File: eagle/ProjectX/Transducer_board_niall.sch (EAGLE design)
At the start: 105 parts, among them T1 MA40S4S, T10 MA40S4S, T100 MA40S4S, T11 MA40S4S, T12 MA40S4S, T13 MA40S4S, T14 MA40S4S, T15 MA40S4S, T16 MA40S4S, T17 MA40S4S, T18 MA40S4S, T19 MA40S4S, T2 MA40S4S, T20 MA40S4S, T21 MA40S4S, T22 MA40S4S, T23 MA40S4S, T24 MA40S4S, T25 MA40S4S, T26 MA40S4S, T27 MA40S4S, T28 MA40S4S, T29 MA40S4S, T3 MA40S4S, T30 MA40S4S, T31 MA40S4S, T32 MA40S4S, T33 MA40S4S, T34 MA40S4S, T35 MA40S4S, T36 MA40S4S, T37 MA40S4S, T38 MA40S4S, T39 MA40S4S, T4 MA40S4S, T40 MA40S4S, T41 MA40S4S, T42 MA40S4S, T43 MA40S4S, T44 MA40S4S, T45 MA40S4S, T46 MA40S4S, T47 MA40S4S, T48 MA40S4S, T49 MA40S4S, T5 MA40S4S, T50 MA40S4S, T51 MA40S4S, T52 MA40S4S, T53 MA40S4S, T54 MA40S4S, T55 MA40S4S, T56 MA40S4S, T57 MA40S4S, T58 MA40S4S, T59 MA40S4S, T6 MA40S4S, T60 MA40S4S, T61 MA40S4S, T62 MA40S4S, T63 MA40S4S, T64 MA40S4S, T65 MA40S4S, T66 MA40S4S, T67 MA40S4S, T68 MA40S4S, T69 MA40S4S, T7 MA40S4S, T70 MA40S4S, T71 MA40S4S, T72 MA40S4S, T73 MA40S4S, T74 MA40S4S, T75 MA40S4S, T76 MA40S4S, T77 MA40S4S, T78 MA40S4S, T79 MA40S4S, T8 MA40S4S, T80 MA40S4S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

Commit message: Niall new board stuff
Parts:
- removed TRANSDUCERS_1, TRANSDUCERS_2, TRANSDUCERS_3, TRANSDUCERS_4, TRANSDUCERS_6: 40_PIN_SMD, Parts:40_PIN_SMD
- added X1, X2, X3, X4, X5: PHB_1MM27_2X20_SNS, _hhn_con_pinhead_box_1mm27:PHB_1MM27_2X20_SNS
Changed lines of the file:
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@@
 <parts>
 <part name="T1" library="Parts" deviceset="MA40S4S" device=""/>
-<part name="TRANSDUCERS_4" library="Parts" deviceset="40_PIN_SMD" device=""/>
-<part name="TRANSDUCERS_3" library="Parts" deviceset="40_PIN_SMD" device=""/>
-<part name="TRANSDUCERS_2" library="Parts" deviceset="40_PIN_SMD" device=""/>
-<part name="TRANSDUCERS_1" library="Parts" deviceset="40_PIN_SMD" device=""/>
 <part name="T2" library="Parts" deviceset="MA40S4S" device=""/>
 <part name="T3" library="Parts" deviceset="MA40S4S" device=""/>
@@
 <part name="T99" library="Parts" deviceset="MA40S4S" device=""/>
 <part name="T100" library="Parts" deviceset="MA40S4S" device=""/>
-<part name="TRANSDUCERS_6" library="Parts" deviceset="40_PIN_SMD" device=""/>
+<part name="X1" library="_hhn_con_pinhead_box_1mm27" deviceset="PHB_1MM27_2X20_*" device="SNS"/>
+<part name="X2" library="_hhn_con_pinhead_box_1mm27" deviceset="PHB_1MM27_2X20_*" device="SNS"/>
+<part name="X3" library="_hhn_con_pinhead_box_1mm27" deviceset="PHB_1MM27_2X20_*" device="SNS"/>
+<part name="X4" library="_hhn_con_pinhead_box_1mm27" deviceset="PHB_1MM27_2X20_*" device="SNS"/>
+<part name="X5" library="_hhn_con_pinhead_box_1mm27" deviceset="PHB_1MM27_2X20_*" device="SNS"/>
 </parts>
 <sheets>
@@
 <instances>
 <instance part="T1" gate="G$1" x="-12.7" y="299.72"/>
-<instance part="TRANSDUCERS_4" gate="G$1" x="175.26" y="27.94" rot="MR0">
-<attribute name="NAME" x="225.298" y="48.26" size="1.778" layer="94" rot="MR0"/>
-</instance>
-<instance part="TRANSDUCERS_3" gate="G$1" x="106.68" y="25.4" rot="MR0">
-<attribute name="NAME" x="156.718" y="45.72" size="1.778" layer="94" rot="MR0"/>
-</instance>
-<instance part="TRANSDUCERS_2" gate="G$1" x="40.64" y="25.4" rot="MR0">
-<attribute name="NAME" x="90.678" y="45.72" size="1.778" layer="94" rot="MR0"/>
-</instance>
-<instance part="TRANSDUCERS_1" gate="G$1" x="-25.4" y="25.4" rot="MR0">
-<attribute name="NAME" x="24.638" y="45.72" size="1.778" layer="94" rot="MR0"/>
-</instance>
 <instance part="T2" gate="G$1" x="10.16" y="299.72"/>
 <instance part="T3" gate="G$1" x="33.02" y="299.72"/>
@@
 <instance part="T99" gate="G$1" x="170.18" y="132.08"/>
 <instance part="T100" gate="G$1" x="195.58" y="132.08"/>
-<instance part="TRANSDUCERS_6" gate="G$1" x="370.84" y="15.24" rot="MR90">
-<attribute name="NAME" x="391.16" y="-34.798" size="1.778" layer="94" rot="MR90"/>
-</instance>
+<instance part="X1" gate="G$1" x="-50.8" y="55.88"/>
+<instance part="X2" gate="G$1" x="-15.24" y="55.88"/>
+<instance part="X3" gate="G$1" x="30.48" y="55.88"/>
+<instance part="X4" gate="G$1" x="78.74" y="55.88"/>
+<instance part="X5" gate="G$1" x="121.92" y="55.88"/>
 </instances>
 <busses>

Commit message: Niall Boards new layout that should slot together
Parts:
- removed X1, X2, X3, X4, X5: PHB_1MM27_2X20_SNS, _hhn_con_pinhead_box_1mm27:PHB_1MM27_2X20_SNS
- added 1, 2, 3, 4: PHB_1MM27_2X25_SNS, _hhn_con_pinhead_box_1mm27:PHB_1MM27_2X25_SNS
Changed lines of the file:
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@@
 <part name="T99" library="Parts" deviceset="MA40S4S" device=""/>
 <part name="T100" library="Parts" deviceset="MA40S4S" device=""/>
-<part name="X1" library="_hhn_con_pinhead_box_1mm27" deviceset="PHB_1MM27_2X20_*" device="SNS"/>
-<part name="X2" library="_hhn_con_pinhead_box_1mm27" deviceset="PHB_1MM27_2X20_*" device="SNS"/>
-<part name="X3" library="_hhn_con_pinhead_box_1mm27" deviceset="PHB_1MM27_2X20_*" device="SNS"/>
-<part name="X4" library="_hhn_con_pinhead_box_1mm27" deviceset="PHB_1MM27_2X20_*" device="SNS"/>
-<part name="X5" library="_hhn_con_pinhead_box_1mm27" deviceset="PHB_1MM27_2X20_*" device="SNS"/>
+<part name="1" library="_hhn_con_pinhead_box_1mm27" deviceset="PHB_1MM27_2X25_*" device="SNS"/>
+<part name="2" library="_hhn_con_pinhead_box_1mm27" deviceset="PHB_1MM27_2X25_*" device="SNS"/>
+<part name="3" library="_hhn_con_pinhead_box_1mm27" deviceset="PHB_1MM27_2X25_*" device="SNS"/>
+<part name="4" library="_hhn_con_pinhead_box_1mm27" deviceset="PHB_1MM27_2X25_*" device="SNS"/>
 </parts>
 <sheets>
@@
 <instance part="T99" gate="G$1" x="170.18" y="132.08"/>
 <instance part="T100" gate="G$1" x="195.58" y="132.08"/>
-<instance part="X1" gate="G$1" x="-50.8" y="55.88"/>
-<instance part="X2" gate="G$1" x="-15.24" y="55.88"/>
-<instance part="X3" gate="G$1" x="30.48" y="55.88"/>
-<instance part="X4" gate="G$1" x="78.74" y="55.88"/>
-<instance part="X5" gate="G$1" x="121.92" y="55.88"/>
+<instance part="1" gate="G$1" x="-106.68" y="248.92" rot="R90"/>
+<instance part="2" gate="G$1" x="-205.74" y="162.56"/>
+<instance part="3" gate="G$1" x="-142.24" y="162.56"/>
+<instance part="4" gate="G$1" x="-78.74" y="160.02"/>
 </instances>
 <busses>

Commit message: Niall board more work
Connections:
- new net FROM_TRANSDUCER_100: 1.50
- new net FROM_TRANSDUCER_85: 1.2
- new net FROM_TRANSDUCER_86: 1.4
- new net FROM_TRANSDUCER_87: 1.6
- new net FROM_TRANSDUCER_88: 1.8
- new net FROM_TRANSDUCER_89: 1.10
- new net FROM_TRANSDUCER_90: 1.12
- new net FROM_TRANSDUCER_91: 1.14
- new net FROM_TRANSDUCER_92: 1.16
- new net FROM_TRANSDUCER_93: 1.36
- new net FROM_TRANSDUCER_94: 1.38
- new net FROM_TRANSDUCER_95: 1.40
- new net FROM_TRANSDUCER_96: 1.42
- new net FROM_TRANSDUCER_97: 1.44
- new net FROM_TRANSDUCER_98: 1.46
- new net FROM_TRANSDUCER_99: 1.48
- new net GND: 1.18, 1.20, 1.22, 1.24, 1.26, 1.28, 1.30, 1.32, 1.34, 2.1, 2.12, 2.13, 2.16, 2.17, 2.20, 2.21, 2.24, 2.25, 2.28, 2.29, 2.32, 2.33, 2.36, 2.37, 2.4, 2.40, 2.41, 2.44, 2.45, 2.48, 2.49, 2.5, 2.8, 2.9, 3.1, 3.12, 3.13, 3.16, 3.17, 3.20, 3.21, 3.24, 3.25, 3.28, 3.29, 3.32, 3.33, 3.36, 3.37, 3.4, 3.40, 3.41, 3.44, 3.45, 3.48, 3.49, 3.5, 3.8, 3.9, 4.1, 4.12, 4.13, 4.16, 4.17, 4.20, 4.21, 4.24, 4.25, 4.28, 4.29, 4.32, 4.33, 4.36, 4.37, 4.4, 4.40, 4.41, 4.44, 4.45, 4.48, 4.49, 4.5, 4.8, 4.9
- new net N$1: T1.1
- new net N$10: T5.2
- new net N$100: T50.2
- new net N$101: T51.1
- new net N$102: T51.2
- new net N$103: T52.1
- new net N$104: T52.2
- new net N$105: T53.1
- new net N$106: T53.2
- new net N$107: T54.1
- new net N$108: T54.2
- new net N$109: T55.1
- new net N$11: T6.1
- new net N$110: T55.2
- new net N$111: T56.1
- new net N$112: T56.2
- new net N$113: T57.1
- new net N$114: T57.2
- new net N$115: T58.1
- new net N$116: T58.2
- new net N$117: T59.1
- new net N$118: T59.2
- new net N$119: T60.1
- new net N$12: T6.2
- new net N$120: T60.2
- new net N$121: T61.1
- new net N$122: T61.2
- new net N$123: T62.1
- new net N$124: T62.2
- new net N$125: T63.1
- new net N$126: T63.2
- new net N$127: T64.1
- new net N$128: T64.2
- new net N$129: T65.1
- new net N$13: T7.1
- new net N$130: T65.2
- new net N$131: T66.1
- new net N$132: T66.2
- new net N$133: T67.1
- new net N$134: T67.2
- new net N$135: T68.1
- new net N$136: T68.2
- new net N$137: T69.1
- new net N$138: T69.2
- new net N$139: T70.1
- new net N$14: T7.2
- new net N$140: T70.2
- new net N$141: T71.1
- new net N$142: T71.2
- new net N$143: T72.1
- new net N$144: T72.2
- new net N$145: T73.1
- new net N$146: T73.2
- new net N$147: T74.1
- new net N$148: T74.2
- new net N$149: T75.1
- new net N$15: T8.1
- new net N$150: T75.2
- new net N$151: T76.1
- new net N$152: T76.2
- new net N$153: T77.1
- new net N$154: T77.2
- new net N$155: T78.1
- new net N$156: T78.2
- new net N$157: T79.1
- new net N$158: T79.2
- new net N$159: T80.1
- new net N$16: T8.2
- new net N$160: T80.2
- new net N$161: T81.1
- new net N$162: T81.2
- new net N$163: T82.1
- new net N$164: T82.2
- new net N$165: T83.1
- new net N$166: T83.2
- new net N$167: T84.1
- new net N$168: T84.2
- new net N$169: T85.1
- new net N$17: T9.1
- new net N$170: T85.2
- new net N$171: T86.1
- new net N$172: T86.2
- new net N$173: T87.1
- new net N$174: T87.2
- new net N$175: T88.1
- new net N$176: T88.2
- new net N$177: T89.1
- new net N$178: T89.2
- new net N$179: T90.1
- new net N$18: T9.2
- new net N$180: T90.2
- new net N$181: T91.1
- new net N$182: T91.2
- new net N$183: T92.1
- new net N$184: T92.2
- new net N$185: T93.1
- new net N$186: T93.2
- new net N$187: T94.1
- new net N$188: T94.2
- new net N$189: T95.1
- new net N$19: T10.1
- new net N$190: T95.2
- new net N$191: T96.1
- new net N$192: T96.2
- new net N$193: T97.1
- new net N$194: T97.2
- new net N$195: T98.1
- new net N$196: T98.2
- new net N$197: T99.1
- new net N$198: T99.2
- new net N$199: T100.1
- new net N$2: T1.2
- new net N$20: T10.2
- new net N$200: T100.2
- new net N$21: T11.1
- new net N$22: T11.2
- new net N$23: T12.1
- new net N$24: T12.2
- new net N$25: T13.1
- new net N$26: T13.2
- new net N$27: T14.1
- new net N$28: T14.2
- new net N$29: T15.1
- new net N$3: T2.1
- new net N$30: T15.2
- new net N$31: T16.1
- new net N$32: T16.2
- new net N$33: T17.1
- new net N$34: T17.2
- new net N$35: T18.1
- new net N$36: T18.2
- new net N$37: T19.1
- new net N$38: T19.2
- new net N$39: T20.1
- new net N$4: T2.2
- new net N$40: T20.2
- new net N$41: T21.1
- new net N$42: T21.2
- new net N$43: T22.1
- new net N$44: T22.2
- new net N$45: T23.1
- new net N$46: T23.2
- new net N$47: T24.1
- new net N$48: T24.2
- new net N$49: T25.1
- new net N$5: T3.1
- new net N$50: T25.2
- new net N$51: T26.1
- new net N$52: T26.2
- new net N$53: T27.1
- new net N$54: T27.2
- new net N$55: T28.1
- new net N$56: T28.2
- new net N$57: T29.1
- new net N$58: T29.2
- new net N$59: T30.1
- new net N$6: T3.2
- new net N$60: T30.2
- new net N$61: T31.1
- new net N$62: T31.2
- new net N$63: T32.1
- new net N$64: T32.2
- new net N$65: T33.1
- new net N$66: T33.2
- new net N$67: T34.1
- new net N$68: T34.2
- new net N$69: T35.1
- new net N$7: T4.1
- new net N$70: T35.2
- new net N$71: T36.1
- new net N$72: T36.2
- new net N$73: T37.1
- new net N$74: T37.2
- new net N$75: T38.1
- new net N$76: T38.2
- new net N$77: T39.1
- new net N$78: T39.2
- new net N$79: T40.1
- new net N$8: T4.2
- new net N$80: T40.2
- new net N$81: T41.1
- new net N$82: T41.2
- new net N$83: T42.1
- new net N$84: T42.2
- new net N$85: T43.1
- new net N$86: T43.2
- new net N$87: T44.1
- new net N$88: T44.2
- new net N$89: T45.1
- new net N$9: T5.1
- new net N$90: T45.2
- new net N$91: T46.1
- new net N$92: T46.2
- new net N$93: T47.1
- new net N$94: T47.2
- new net N$95: T48.1
- new net N$96: T48.2
- new net N$97: T49.1
- new net N$98: T49.2
- new net N$99: T50.1
- new net TO_TRANSDUCER_100: 1.49
- new net TO_TRANSDUCER_76: 1.17
- new net TO_TRANSDUCER_77: 1.19
- new net TO_TRANSDUCER_78: 1.21
- new net TO_TRANSDUCER_79: 1.23
- new net TO_TRANSDUCER_80: 1.25
- new net TO_TRANSDUCER_81: 1.27
- new net TO_TRANSDUCER_82: 1.29
- new net TO_TRANSDUCER_83: 1.31
- new net TO_TRANSDUCER_84: 1.33
- new net TO_TRANSDUCER_85: 1.1
- new net TO_TRANSDUCER_86: 1.3
- new net TO_TRANSDUCER_87: 1.5
- new net TO_TRANSDUCER_88: 1.7
- new net TO_TRANSDUCER_89: 1.9
- new net TO_TRANSDUCER_90: 1.11
- new net TO_TRANSDUCER_91: 1.13
- new net TO_TRANSDUCER_92: 1.15
- new net TO_TRANSDUCER_93: 1.35
- new net TO_TRANSDUCER_94: 1.37
- new net TO_TRANSDUCER_95: 1.39
- new net TO_TRANSDUCER_96: 1.41
- new net TO_TRANSDUCER_97: 1.43
- new net TO_TRANSDUCER_98: 1.45
- new net TO_TRANSDUCER_99: 1.47
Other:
- moved on the sheet: 1, 2, 3, 4

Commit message: Transducer board start
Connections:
- net N$10 renamed TO_T_5
- net N$101 renamed FROM_T_51
- net N$102 renamed TO_T_51
- net N$107 renamed FROM_T_54
- net N$108 renamed TO_T_54
- net N$113 renamed FROM_T_57
- net N$114 renamed TO_T_57
- net N$115 renamed FROM_T_58
- net N$116 renamed TO_T_58
- net N$117 renamed FROM_T_59
- net N$118 renamed TO_T_59
- net N$121 renamed FROM_T_61
- net N$122 renamed TO_T_61
- net N$123 renamed FROM_T_62
- net N$124 renamed TO_T_62
- net N$125 renamed FROM_T_63
- net N$126 renamed TO_T_63
- net N$127 renamed FROM_T_64
- net N$128 renamed TO_T_64
- net N$129 renamed FROM_T_65
- net N$13 renamed FROM_T_7
- net N$130 renamed TO_T_65
- net N$131 renamed FROM_T_66
- net N$132 renamed TO_T_66
- net N$133 renamed FROM_T_67
- net N$134 renamed TO_T_67
- net N$139 renamed FROM_T_70
- net N$14 renamed TO_T_7
- net N$140 renamed TO_T_70
- net N$141 renamed FROM_T_71
- net N$142 renamed TO_T_71
- net N$147 renamed FROM_T_74
- net N$148 renamed TO_T_74
- net N$149 renamed FROM_T_75
- net N$15 renamed FROM_T_8
- net N$150 renamed TO_T_75
- net N$151 renamed FROM_T_76
- net N$152 renamed TO_T_76
- net N$153 renamed FROM_T_77
- net N$154 renamed TO_T_77
- net N$155 renamed FROM_T_78
- net N$156 renamed TO_T_78
- net N$159 renamed FROM_T_80
- net N$16 renamed TO_T_8
- net N$160 renamed TO_T_80
- net N$161 renamed FROM_T_81
- net N$162 renamed TO_T_81
- net N$163 renamed FROM_T_82
- net N$164 renamed TO_T_82
- net N$165 renamed FROM_T_83
- net N$166 renamed TO_T_83
- net N$167 renamed FROM_T_84
- net N$168 renamed TO_T_84
- net N$169 renamed FROM_T_85
- net N$17 renamed FROM_T_9
- net N$170 renamed TO_T_85
- net N$171 renamed FROM_T_86
- net N$172 renamed TO_T_86
- net N$173 renamed FROM_T_87
- net N$174 renamed TO_T_87
- net N$179 renamed FROM_T_90
- net N$18 renamed TO_T_9
- net N$180 renamed TO_T_90
- net N$187 renamed FROM_T_94
- net N$188 renamed TO_T_94
- net N$189 renamed FROM_T_95
- net N$190 renamed TO_T_95
- net N$193 renamed FROM_T_97
- net N$194 renamed TO_T_97
- net N$195 renamed FROM_T_98
- net N$196 renamed TO_T_98
- net N$197 renamed FROM_T_99
- net N$198 renamed TO_T_99
- net N$21 renamed FROM_T_11
- net N$22 renamed TO_T_11
- net N$23 renamed FROM_T_12
- net N$24 renamed TO_T_12
- net N$25 renamed FROM_T_13
- net N$26 renamed TO_T_13
- net N$27 renamed FROM_T_14
- net N$28 renamed TO_T_14
- net N$29 renamed FROM_T_15
- net N$3 renamed FROM_T_2
- net N$30 renamed TO_T_15
- net N$31 renamed FROM_T_16
- net N$32 renamed TO_T_16
- net N$33 renamed FROM_T_17
- net N$34 renamed TO_T_17
- net N$35 renamed FROM_T_18
- net N$36 renamed TO_T_18
- net N$37 renamed FROM_T_19
- net N$38 renamed TO_T_19
- net N$39 renamed FROM_T_20
- net N$4 renamed TO_T_2
- net N$40 renamed TO_T_20
- net N$41 renamed FROM_T_21
- net N$42 renamed TO_T_21
- net N$45 renamed FROM_T_23
- net N$46 renamed TO_T_23
- net N$47 renamed FROM_T_24
- net N$48 renamed TO_T_24
- net N$49 renamed FROM_T_25
- net N$5 renamed FROM_T_3
- net N$50 renamed TO_T_25
- net N$51 renamed FROM_T_26
- net N$52 renamed TO_T_26
- net N$53 renamed FROM_T_27
- net N$54 renamed TO_T_27
- net N$57 renamed FROM_T_29
- net N$58 renamed TO_T_29
- net N$59 renamed FROM_T_30
- net N$6 renamed TO_T_3
- net N$60 renamed TO_T_30
- net N$61 renamed FROM_T_31
- net N$62 renamed TO_T_31
- net N$63 renamed FROM_T_32
- net N$64 renamed TO_T_32
- net N$65 renamed FROM_T_33
- net N$66 renamed TO_T_33
- net N$67 renamed FROM_T_34
- net N$68 renamed TO_T_34
- net N$69 renamed FROM_T_35
- net N$7 renamed FROM_T_4
- net N$70 renamed TO_T_35
- net N$71 renamed FROM_T_36
- net N$72 renamed TO_T_36
- net N$73 renamed FROM_T_37
- net N$74 renamed TO_T_37
- net N$75 renamed FROM_T_38
- net N$76 renamed TO_T_38
- net N$77 renamed FROM_T_39
- net N$78 renamed TO_T_39
- net N$79 renamed FROM_T_40
- net N$8 renamed TO_T_4
- net N$80 renamed TO_T_40
- net N$81 renamed FROM_T_41
- net N$82 renamed TO_T_41
- net N$83 renamed FROM_T_42
- net N$84 renamed TO_T_42
- net N$85 renamed FROM_T_43
- net N$86 renamed TO_T_43
- net N$87 renamed FROM_T_44
- net N$88 renamed TO_T_44
- net N$9 renamed FROM_T_5
- net N$93 renamed FROM_T_47
- net N$94 renamed TO_T_47
- net N$95 renamed FROM_T_48
- net N$96 renamed TO_T_48
- net N$97 renamed FROM_T_49
- net N$98 renamed TO_T_49
- removed net FROM_TRANSDUCER_100: 1.50
- removed net FROM_TRANSDUCER_85: 1.2
- removed net FROM_TRANSDUCER_86: 1.4
- removed net FROM_TRANSDUCER_87: 1.6
- removed net FROM_TRANSDUCER_88: 1.8
- removed net FROM_TRANSDUCER_89: 1.10
- removed net FROM_TRANSDUCER_90: 1.12
- removed net FROM_TRANSDUCER_91: 1.14
- removed net FROM_TRANSDUCER_92: 1.16
- removed net FROM_TRANSDUCER_93: 1.36
- removed net FROM_TRANSDUCER_94: 1.38
- removed net FROM_TRANSDUCER_95: 1.40
- removed net FROM_TRANSDUCER_96: 1.42
- removed net FROM_TRANSDUCER_97: 1.44
- removed net FROM_TRANSDUCER_98: 1.46
- removed net FROM_TRANSDUCER_99: 1.48
- removed net GND: 1.18, 1.20, 1.22, 1.24, 1.26, 1.28, 1.30, 1.32, 1.34, 2.1, 2.12, 2.13, 2.16, 2.17, 2.20, 2.21, 2.24, 2.25, 2.28, 2.29, 2.32, 2.33, 2.36, 2.37, 2.4, 2.40, 2.41, 2.44, 2.45, 2.48, 2.49, 2.5, 2.8, 2.9, 3.1, 3.12, 3.13, 3.16, 3.17, 3.20, 3.21, 3.24, 3.25, 3.28, 3.29, 3.32, 3.33, 3.36, 3.37, 3.4, 3.40, 3.41, 3.44, 3.45, 3.48, 3.49, 3.5, 3.8, 3.9, 4.1, 4.12, 4.13, 4.16, 4.17, 4.20, 4.21, 4.24, 4.25, 4.28, 4.29, 4.32, 4.33, 4.36, 4.37, 4.4, 4.40, 4.41, 4.44, 4.45, 4.48, 4.49, 4.5, 4.8, 4.9
- removed net N$1: T1.1
- removed net N$100: T50.2
- removed net N$103: T52.1
- removed net N$104: T52.2
- removed net N$105: T53.1
- removed net N$106: T53.2
- removed net N$109: T55.1
- removed net N$11: T6.1
- removed net N$110: T55.2
- removed net N$111: T56.1
- removed net N$112: T56.2
- removed net N$119: T60.1
- removed net N$12: T6.2
- removed net N$120: T60.2
- removed net N$135: T68.1
- removed net N$136: T68.2
- removed net N$137: T69.1
- removed net N$138: T69.2
- removed net N$143: T72.1
- removed net N$144: T72.2
- removed net N$145: T73.1
- removed net N$146: T73.2
- removed net N$157: T79.1
- removed net N$158: T79.2
- removed net N$175: T88.1
- removed net N$176: T88.2
- removed net N$177: T89.1
- removed net N$178: T89.2
- removed net N$181: T91.1
- removed net N$182: T91.2
- removed net N$183: T92.1
- removed net N$184: T92.2
- removed net N$185: T93.1
- removed net N$186: T93.2
- removed net N$19: T10.1
- removed net N$191: T96.1
- removed net N$192: T96.2
- removed net N$199: T100.1
- removed net N$2: T1.2
- removed net N$20: T10.2
- removed net N$200: T100.2
- removed net N$43: T22.1
- removed net N$44: T22.2
- removed net N$55: T28.1
- removed net N$56: T28.2
- removed net N$89: T45.1
- removed net N$90: T45.2
- removed net N$91: T46.1
- removed net N$92: T46.2
- removed net N$99: T50.1
- removed net TO_TRANSDUCER_100: 1.49
- removed net TO_TRANSDUCER_76: 1.17
- removed net TO_TRANSDUCER_77: 1.19
- removed net TO_TRANSDUCER_78: 1.21
- removed net TO_TRANSDUCER_79: 1.23
- removed net TO_TRANSDUCER_80: 1.25
- removed net TO_TRANSDUCER_81: 1.27
- removed net TO_TRANSDUCER_82: 1.29
- removed net TO_TRANSDUCER_83: 1.31
- removed net TO_TRANSDUCER_84: 1.33
- removed net TO_TRANSDUCER_85: 1.1
- removed net TO_TRANSDUCER_86: 1.3
- removed net TO_TRANSDUCER_87: 1.5
- removed net TO_TRANSDUCER_88: 1.7
- removed net TO_TRANSDUCER_89: 1.9
- removed net TO_TRANSDUCER_90: 1.11
- removed net TO_TRANSDUCER_91: 1.13
- removed net TO_TRANSDUCER_92: 1.15
- removed net TO_TRANSDUCER_93: 1.35
- removed net TO_TRANSDUCER_94: 1.37
- removed net TO_TRANSDUCER_95: 1.39
- removed net TO_TRANSDUCER_96: 1.41
- removed net TO_TRANSDUCER_97: 1.43
- removed net TO_TRANSDUCER_98: 1.45
- removed net TO_TRANSDUCER_99: 1.47
- new net FROM_T_1: 1.2, T1.1
- new net FROM_T_10: 1.6, T10.1
- new net FROM_T_100: 1.48, T100.1
- new net FROM_T_22: 1.40, T22.1
- new net FROM_T_28: 1.12, T28.1
- new net FROM_T_45: 1.14, T45.1
- new net FROM_T_46: 1.16, T46.1
- new net FROM_T_50: 1.8, T50.1
- new net FROM_T_52: 1.22, T52.1
- new net FROM_T_53: 1.24, T53.1
- new net FROM_T_55: 1.36, T55.1
- new net FROM_T_56: 1.38, T56.1
- new net FROM_T_6: 1.4, T6.1
- new net FROM_T_60: 1.10, T60.1
- new net FROM_T_68: 1.20, T68.1
- new net FROM_T_69: 1.26, T69.1
- new net FROM_T_72: 1.42, T72.1
- new net FROM_T_73: 1.18, T73.1
- new net FROM_T_79: 1.44, T79.1
- new net FROM_T_88: 1.30, T88.1
- new net FROM_T_89: 1.28, T89.1
- new net FROM_T_91: 1.50, T91.1
- new net FROM_T_92: 1.32, T92.1
- new net FROM_T_93: 1.34, T93.1
- new net FROM_T_96: 1.46, T96.1
- new net TO_T_1: 1.1, T1.2
- new net TO_T_10: 1.5, T10.2
- new net TO_T_100: 1.47, T100.2
- new net TO_T_22: 1.39, T22.2
- new net TO_T_28: 1.11, T28.2
- new net TO_T_45: 1.13, T45.2
- new net TO_T_46: 1.15, T46.2
- new net TO_T_50: 1.7, T50.2
- new net TO_T_52: 1.21, T52.2
- new net TO_T_53: 1.23, T53.2
- new net TO_T_55: 1.35, T55.2
- new net TO_T_56: 1.37, T56.2
- new net TO_T_6: 1.3, T6.2
- new net TO_T_60: 1.9, T60.2
- new net TO_T_68: 1.19, T68.2
- new net TO_T_69: 1.25, T69.2
- new net TO_T_72: 1.41, T72.2
- new net TO_T_73: 1.17, T73.2
- new net TO_T_79: 1.43, T79.2
- new net TO_T_88: 1.29, T88.2
- new net TO_T_89: 1.27, T89.2
- new net TO_T_91: 1.49, T91.2
- new net TO_T_92: 1.31, T92.2
- new net TO_T_93: 1.33, T93.2
- new net TO_T_96: 1.45, T96.2
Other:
- note added: "Transievers Green"

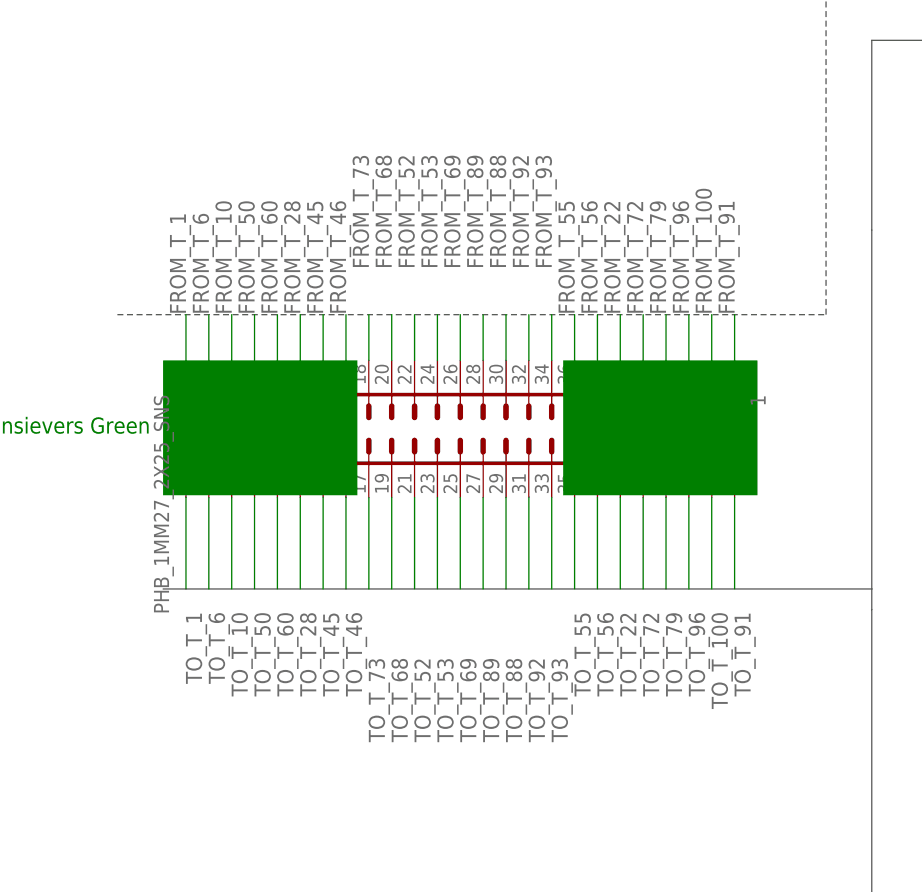
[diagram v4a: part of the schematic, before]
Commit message: Transievers routed
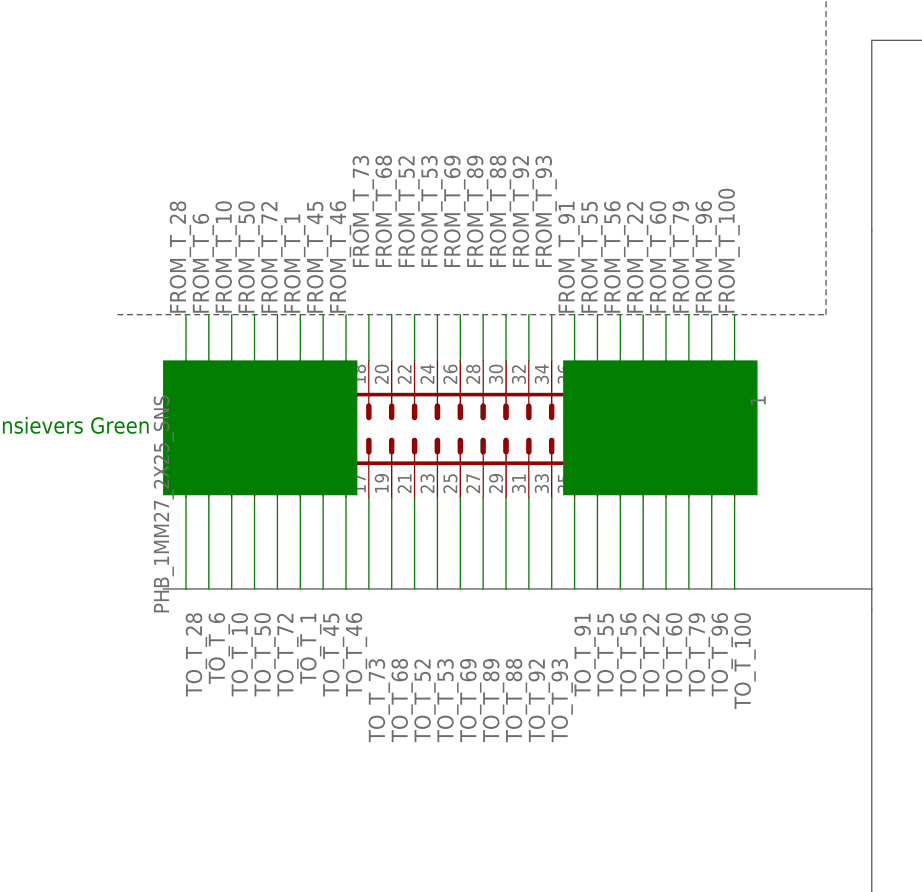
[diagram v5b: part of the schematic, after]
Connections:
- net FROM_T_1: now also 1.12; no longer 1.2
- net FROM_T_100: now also 1.50; no longer 1.48
- net FROM_T_22: now also 1.42; no longer 1.40
- net FROM_T_28: now also 1.2; no longer 1.12
- net FROM_T_55: now also 1.38; no longer 1.36
- net FROM_T_56: now also 1.40; no longer 1.38
- net FROM_T_60: now also 1.44; no longer 1.10
- net FROM_T_72: now also 1.10; no longer 1.42
- net FROM_T_79: now also 1.46; no longer 1.44
- net FROM_T_91: now also 1.36; no longer 1.50
- net FROM_T_96: now also 1.48; no longer 1.46
- net TO_T_1: now also 1.11; no longer 1.1
- net TO_T_100: now also 1.49; no longer 1.47
- net TO_T_22: now also 1.41; no longer 1.39
- net TO_T_28: now also 1.1; no longer 1.11
- net TO_T_55: now also 1.37; no longer 1.35
- net TO_T_56: now also 1.39; no longer 1.37
- net TO_T_60: now also 1.43; no longer 1.9
- net TO_T_72: now also 1.9; no longer 1.41
- net TO_T_79: now also 1.45; no longer 1.43
- net TO_T_91: now also 1.35; no longer 1.49
- net TO_T_96: now also 1.47; no longer 1.45

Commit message: More board work
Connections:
- net FROM_T_17: now also 4.17
- net FROM_T_18: now also 4.12
- net FROM_T_19: now also 4.5
- net FROM_T_2: now also 4.8
- net FROM_T_20: now also 4.4
- net FROM_T_21: now also 4.1
- net FROM_T_23: now also 4.9
- net FROM_T_24: now also 4.16
- net FROM_T_3: now also 4.13
- net FROM_T_4: now also 4.20
- net FROM_T_49: now also 1.18
- net FROM_T_51: now also 1.24
- net FROM_T_52: now also 1.20; no longer 1.22
- net FROM_T_53: no longer 1.24
- net FROM_T_68: no longer 1.20
- net FROM_T_69: now also 1.22; no longer 1.26
- net FROM_T_70: now also 1.26
- net FROM_T_71: now also 1.28
- net FROM_T_73: no longer 1.18
- net FROM_T_88: no longer 1.30
- net FROM_T_89: now also 1.32; no longer 1.28
- net FROM_T_90: now also 1.30
- net FROM_T_92: now also 1.34; no longer 1.32
- net FROM_T_93: no longer 1.34
- net TO_T_17: now also 4.18
- net TO_T_18: now also 4.11
- net TO_T_19: now also 4.6
- net TO_T_2: now also 4.7
- net TO_T_20: now also 4.3
- net TO_T_21: now also 4.2
- net TO_T_23: now also 4.10
- net TO_T_24: now also 4.15
- net TO_T_3: now also 4.14
- net TO_T_4: now also 4.19
- net TO_T_49: now also 1.17
- net TO_T_51: now also 1.23
- net TO_T_52: now also 1.19; no longer 1.21
- net TO_T_53: no longer 1.23
- net TO_T_68: no longer 1.19
- net TO_T_69: now also 1.21; no longer 1.25
- net TO_T_70: now also 1.25
- net TO_T_71: now also 1.27
- net TO_T_73: no longer 1.17
- net TO_T_88: no longer 1.29
- net TO_T_89: now also 1.31; no longer 1.27
- net TO_T_90: now also 1.29
- net TO_T_92: now also 1.33; no longer 1.31
- net TO_T_93: no longer 1.33
